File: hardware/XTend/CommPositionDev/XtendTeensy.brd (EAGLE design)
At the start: 100 x 63 mm, 43 parts, among them J1 POWER_JACK, J2 HIROSE_DM3CS-SF, J3 JST_SM05B, SW1 SPDT_RA_3A, U1 TXB0108PWR, U2 5510003828F, U3 LM60, U4 COPERNICUS_II_DIP, U5 TEENSY_3.X, U6 7805T

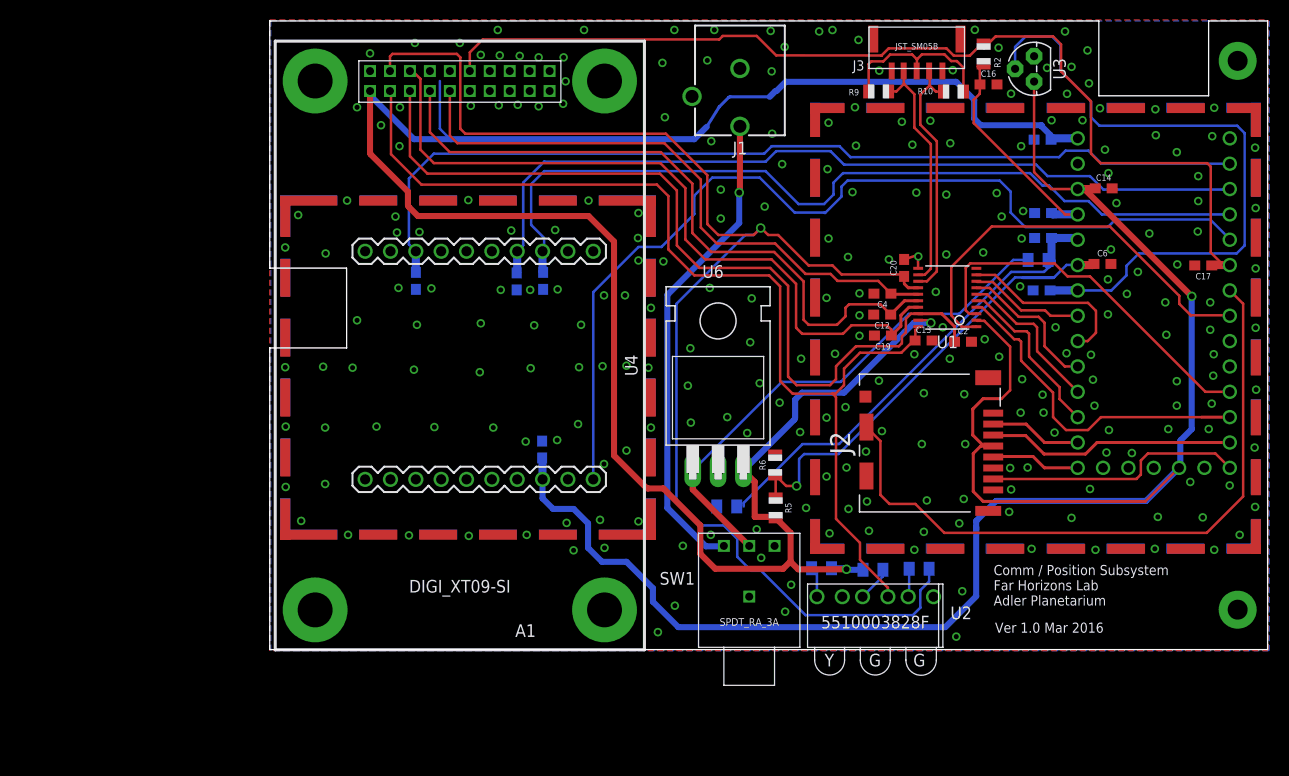
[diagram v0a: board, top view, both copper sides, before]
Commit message: Update to state of XTendTeensy at move to FHComm repo
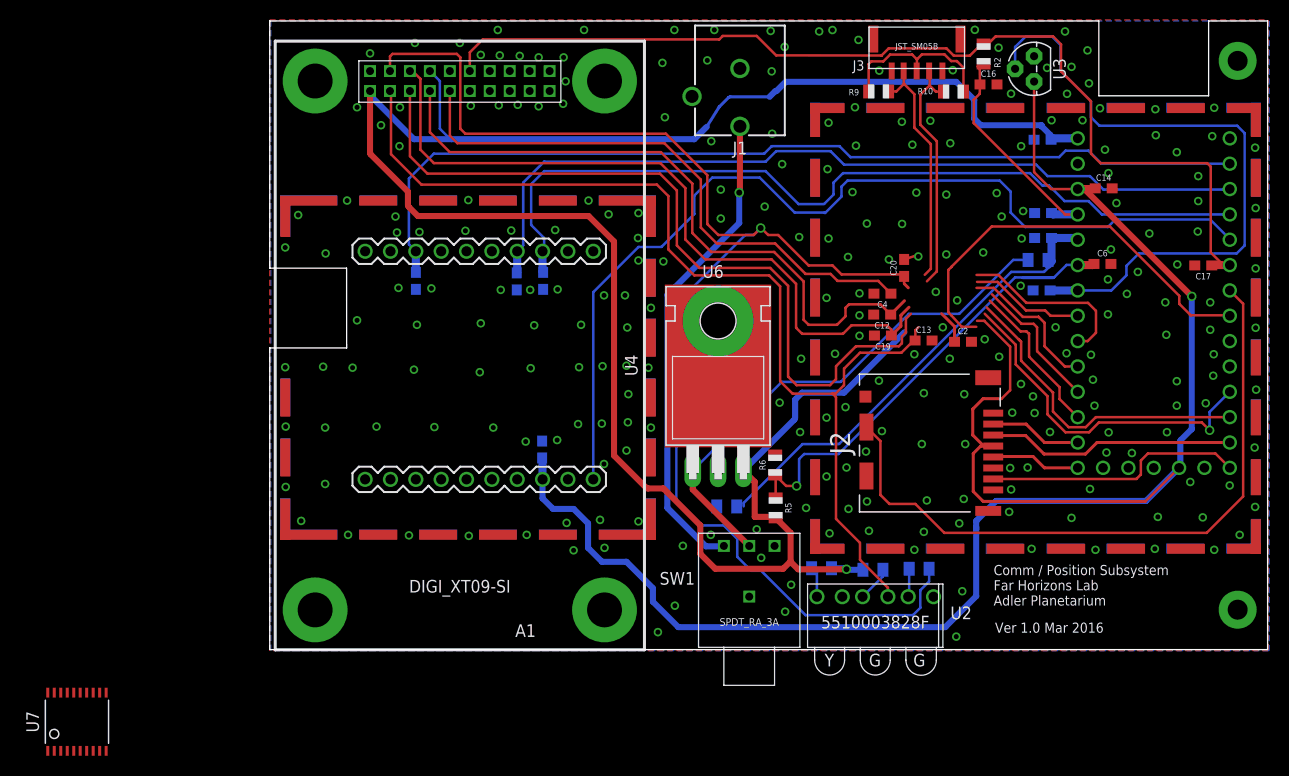
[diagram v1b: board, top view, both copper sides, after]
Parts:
- removed U1: TXB0108PWR, adafruit-fh:TSSOP20
- added U7: TXB0108PWR, adafruit-fh:TSSOP20
- C11: value 30pF -> 0.22uF
- R2: value (none) -> 10k
- SHLD3: value BMI-S-2XX1 -> BMI-S-2XX4; device fhmechanical:BMI-S-206-F -> fhmechanical:BMI-S-206-F_COPERNICUS
- SHLD4: value BMI-S-2XX1 -> BMI-S-2XX5; device fhmechanical:BMI-S-206-F -> fhmechanical:BMI-S-206-F_COPERNICUS_M
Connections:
- removed net N$15: U1.1, U5.6
- removed net N$23: U1.5, U5.15/A1
- removed net N$24: U1.6, U5.16/A2
- removed net N$25: U1.4, U5.10
- removed net N$26: U1.7, U5.17/A3
- removed net N$4: U1.3, U5.9
- removed net N$6: U1.9, U5.18/A4
- removed net N$9: U1.8, U5.19/A5
- net 3.3V: no longer U1.2
- net 5.0V: now also A1.P$7; no longer U1.19
- net GND: now also U6.MOUNT, U6.TAB; no longer A1.P$7, SHLD3.P$1, SHLD3.P$9, SHLD4.P$10, SHLD4.P$11, U1.11
- net N$11: now also U5.16/A2; no longer U1.15
- net N$12: now also U5.6; no longer U1.20
- net N$13: now also U5.15/A1; no longer U1.16
- net N$14: now also U5.17/A3; no longer U1.14
- net N$5: now also U5.10; no longer U1.17
- net N$8: now also U5.9; no longer U1.18
- net SCL: now also U5.19/A5; no longer U1.13
- net SDA: now also U5.18/A4; no longer U1.12
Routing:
- net N$12: track 104.8 -> 146.7 mm
- net N$15: track 41.6 -> 0.00 mm
- net N$4: track 37.5 -> 0.00 mm
- net N$25: track 33.6 -> 0.00 mm
- net N$8: track 86.2 -> 118.2 mm, vias 0 -> 1
- net N$5: track 74.5 -> 105.8 mm
- net N$6: track 17.9 -> 0.00 mm
- net SDA: track 24.3 -> 41.5 mm
- net N$23: track 17.0 -> 0.00 mm
- net N$24: track 15.6 -> 0.00 mm
- net N$26: track 14.8 -> 0.00 mm
- net N$13: track 68.6 -> 82.9 mm
- net N$14: track 138.5 -> 152.3 mm
- net N$9: track 11.6 -> 0.00 mm
- net N$11: track 60.9 -> 72.2 mm
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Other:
- board text added: "Remove mirrored labels, values SPDT Switch has wrong package X GPS Connector cutout skipped Mirror GPS and use taller shield on connector side Use machined sockets for modules X Level Translator OE must be high, preferably after supplies are stable. X A1 SHDN* should be tied HIGH. X Drill hole and expose GND for U6 tab. Add Battery for Teensy RTC & GPS Add another LED module. Add 30pf bypasses to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"
